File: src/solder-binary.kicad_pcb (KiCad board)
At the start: 2 copper layers, 90 x 82 mm, 45 parts, among them J1 Energy, J2 Conn_01x03_Socket, J3 Conn_01x06_Socket, J4 Conn_01x06_Socket, J5 Conn_02x04_Odd_Even, J6 Conn_01x04_Pin, Q1 2N3906, Q2 2N3904, Q3 2N3906, Q4 2N3904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

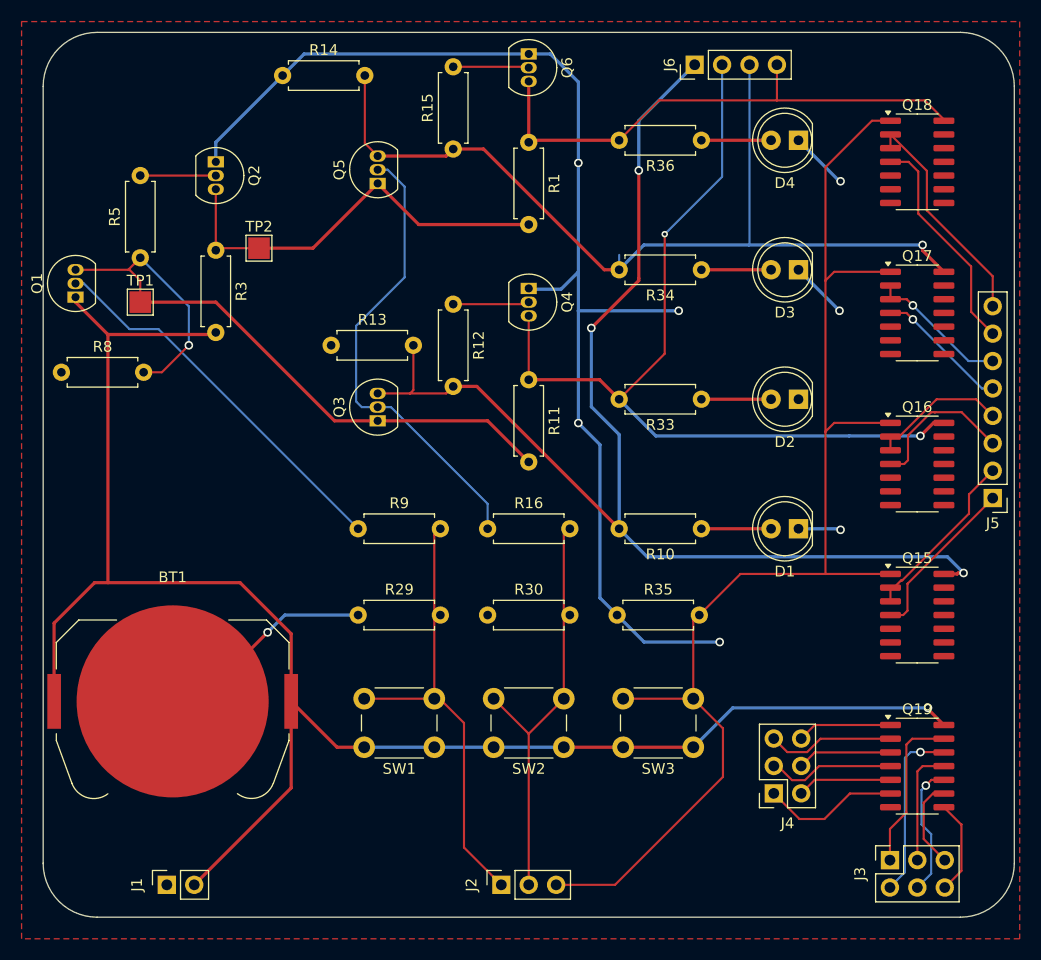
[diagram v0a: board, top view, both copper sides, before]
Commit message: Update source files with silkscreen
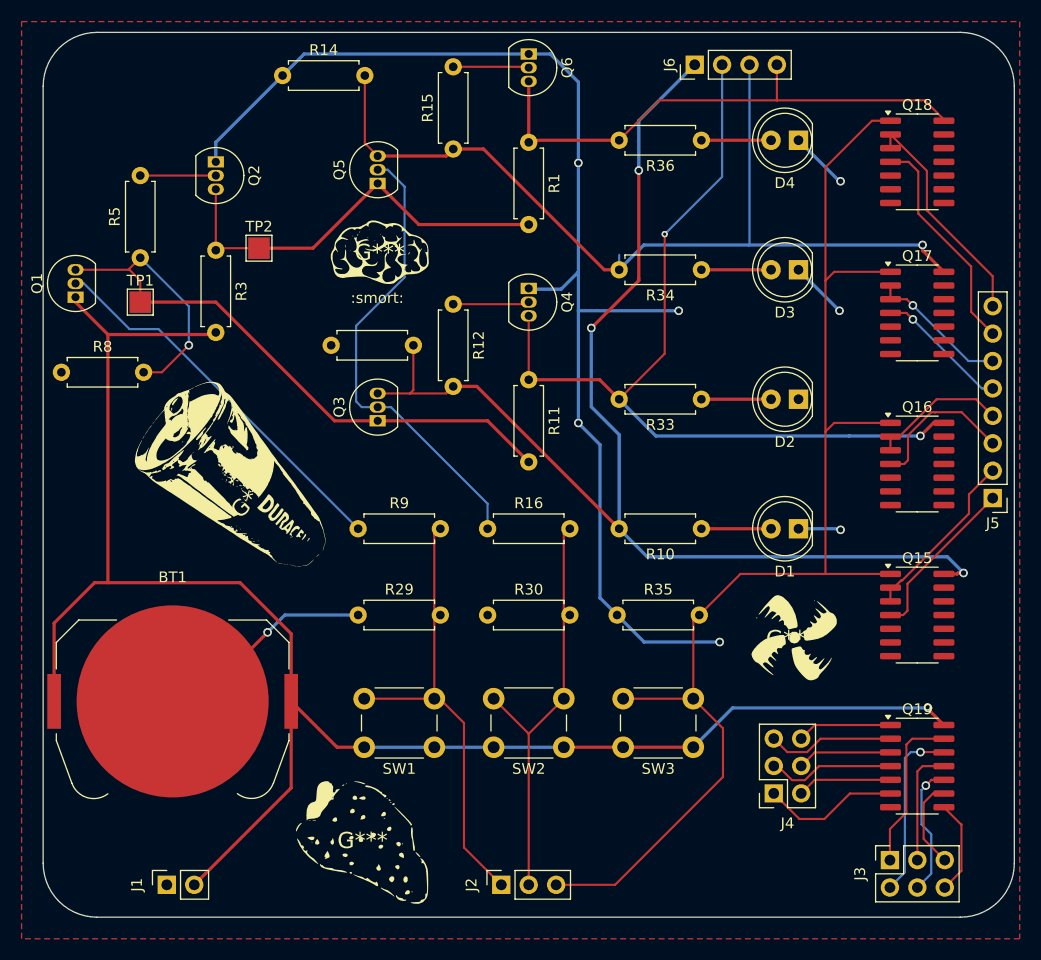
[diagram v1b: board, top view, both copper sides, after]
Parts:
- added G***: LOGO, LOGO, F.Cu at (128.2, 46.4)
- added G***: LOGO, LOGO, F.Cu at (166.3, 82.2)
- added G***: LOGO, LOGO, F.Cu at (126.6, 100.9)
- added G***: LOGO, LOGO, F.Cu at (116.4, 69.0)
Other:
- board text added: ":smort:"
